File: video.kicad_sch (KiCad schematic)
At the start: 8 parts, among them U20 THS7374

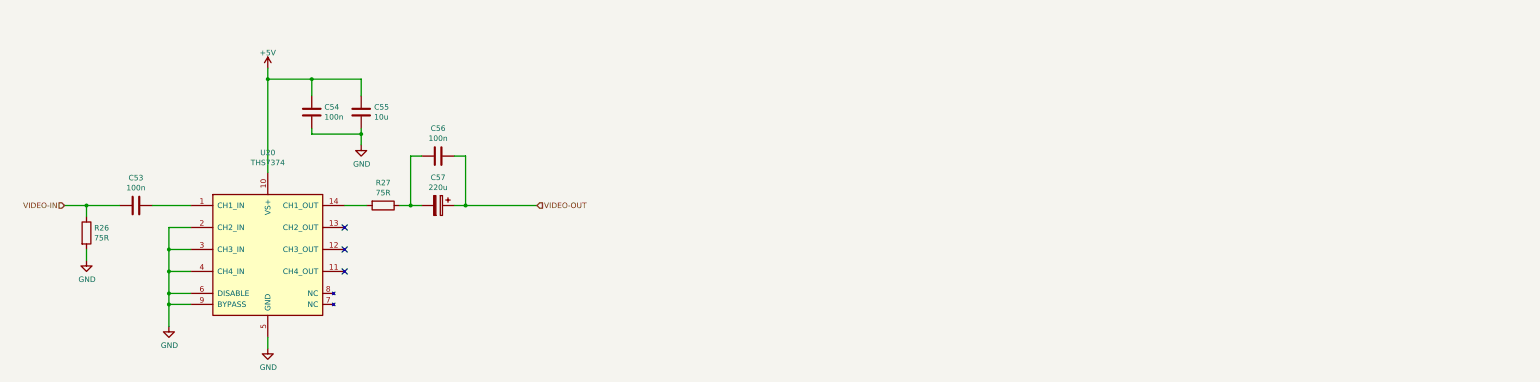
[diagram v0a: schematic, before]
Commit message: rev2 sent to fab
Added CHR RAM.
Changed board to 4 layers (was 2 layers).
Changed passives to 0603 (was 0402)
Fixed CIRAM-A10 not being hooked up
Fixed PPU-A10..A12 being hooked to VRAM but should have been.
Added more silkscreen for easier debugging.
Added filter inductor to 5V from USB-C.
Changed video out to stock (was THS7374)
Changed audio circuit to stock (was headphone amp IC)
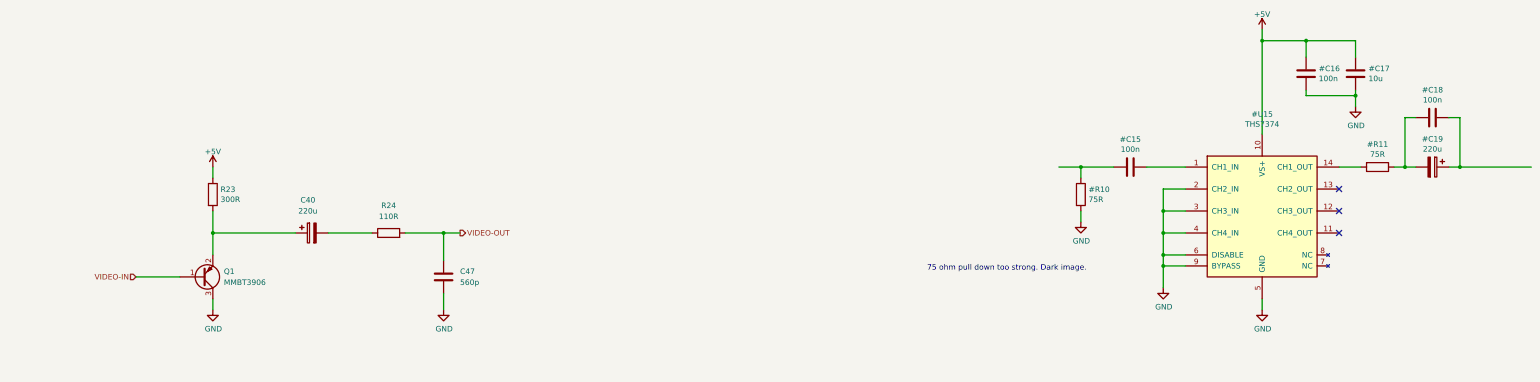
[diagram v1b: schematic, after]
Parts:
- added C40: 220u, Capacitor_Tantalum_SMD:CP_EIA-7343-15_Kemet-W, symbol Device:C_Polarized
- added C47: 560p, Capacitor_SMD:C_0603_1608Metric_Pad1.08x0.95mm_HandSolder, symbol Device:C
- added Q1: MMBT3906, Package_TO_SOT_SMD:SOT-23, symbol Transistor_BJT:MMBT3906
- added R23: 300R, Resistor_SMD:R_0603_1608Metric_Pad0.98x0.95mm_HandSolder, symbol Device:R
- added R24: 110R, Resistor_SMD:R_0603_1608Metric_Pad0.98x0.95mm_HandSolder, symbol Device:R
- #C15: renamed from C53; footprint Capacitor_SMD:C_0402_1005Metric -> Capacitor_SMD:C_0603_1608Metric_Pad1.08x0.95mm_HandSolder; Digikey 1276-1509-2-ND -> (none); MPN CL05B104KO5NNWC -> (none)
- #C16: renamed from C54; footprint Capacitor_SMD:C_0402_1005Metric -> Capacitor_SMD:C_0603_1608Metric_Pad1.08x0.95mm_HandSolder; Digikey 1276-1509-2-ND -> (none); MPN CL05B104KO5NNWC -> (none)
- #C17: renamed from C55; footprint Capacitor_SMD:C_0805_2012Metric -> Capacitor_SMD:C_0805_2012Metric_Pad1.18x1.45mm_HandSolder
- #C18: renamed from C56; footprint Capacitor_SMD:C_0402_1005Metric -> Capacitor_SMD:C_0603_1608Metric_Pad1.08x0.95mm_HandSolder; Digikey 1276-1509-2-ND -> (none); MPN CL05B104KO5NNWC -> (none)
- #R10: renamed from R26; footprint Resistor_SMD:R_0402_1005Metric -> Resistor_SMD:R_0603_1608Metric_Pad0.98x0.95mm_HandSolder; Digikey P75.0LCT-ND -> (none); MPN ERJ-2RKF75R0X -> (none)
- #R11: renamed from R27; footprint Resistor_SMD:R_0402_1005Metric -> Resistor_SMD:R_0603_1608Metric_Pad0.98x0.95mm_HandSolder; Digikey P75.0LCT-ND -> (none); MPN ERJ-2RKF75R0X -> (none)
- renumbered C57 to #C19, U20 to #U15
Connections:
- net +5V: now also R23.1
- net GND: now also C47.2, Q1.3 (C)
- net VIDEO-IN: now also Q1.1 (B); no longer #C15.2, #R10.1
- net VIDEO-OUT: now also C47.1, R24.2; no longer #C18.1, #C19.1
- new net: #C18.1, #C19.1
- new net: #C15.2, #R10.1
- new net: C40.1, Q1.2 (E), R23.2
- new net: C40.2, R24.1
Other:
- note added: "75 ohm pull down too strong. Dark image."

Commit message: filled out BOM
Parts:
- C40: Digikey (none) -> 478-11218-1-ND; MPN (none) -> TAJD227K010TNJV
- C47: Digikey (none) -> 399-C0603C561J5GAC7867CT-ND; MPN (none) -> C0603C561J5GAC7867
- Q1: Digikey (none) -> BC857CLT1GOSCT-ND; MPN MMBT3906 -> BC857CLT1G
- R23: Digikey (none) -> RMCF0603FT300RCT-ND; MPN (none) -> RMCF0603FT300R
- R24: Digikey (none) -> RMCF0603FT110RCT-ND; MPN (none) -> RMCF0603FT110R
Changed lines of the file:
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@@
   (title_block
     (title "InGame-NES MMC3")
-    (date "2022-06-03")
-    (rev "1")
+    (date "2022-08-02")
+    (rev "2")
     (company "Late to the Game")
   )
@@
       (effects (font (size 1.27 1.27)) hide)
     )
-    (property "Description" "" (id 4) (at 129.54 82.55 0)
-      (effects (font (size 1.27 1.27)) hide)
-    )
-    (property "Digikey" "" (id 5) (at 129.54 82.55 0)
-      (effects (font (size 1.27 1.27)) hide)
-    )
-    (property "MPN" "" (id 6) (at 129.54 82.55 0)
+    (property "Description" "RES SMD 300 OHM 1% 1/10W 0603" (id 4) (at 129.54 82.55 0)
+      (effects (font (size 1.27 1.27)) hide)
+    )
+    (property "Digikey" "RMCF0603FT300RCT-ND" (id 5) (at 129.54 82.55 0)
+      (effects (font (size 1.27 1.27)) hide)
+    )
+    (property "MPN" "RMCF0603FT300R" (id 6) (at 129.54 82.55 0)
       (effects (font (size 1.27 1.27)) hide)
     )
@@
       (effects (font (size 1.27 1.27)) hide)
     )
-    (property "Digikey" "" (id 5) (at 152.4 91.44 0)
-      (effects (font (size 1.27 1.27)) hide)
-    )
-    (property "MPN" "" (id 6) (at 152.4 91.44 0)
+    (property "Digikey" "478-11218-1-ND" (id 5) (at 152.4 91.44 0)
+      (effects (font (size 1.27 1.27)) hide)
+    )
+    (property "MPN" "TAJD227K010TNJV" (id 6) (at 152.4 91.44 0)
       (effects (font (size 1.27 1.27)) hide)
     )
@@
       (effects (font (size 1.27 1.27)) hide)
     )
-    (property "Description" "CAP CER 0.1UF 16V X7R 0603" (id 4) (at 182.88 101.6 0)
+    (property "Description" "CAP CER 560PF 50V C0G/NP0 0603" (id 4) (at 182.88 101.6 0)
       (effects (font (size 1.27 1.27)) hide)
     )
@@
       (effects (font (size 1.27 1.27)) hide)
     )
-    (property "Digikey" "" (id 6) (at 182.88 101.6 0)
-      (effects (font (size 1.27 1.27)) hide)
-    )
-    (property "MPN" "" (id 7) (at 182.88 101.6 0)
+    (property "Digikey" "399-C0603C561J5GAC7867CT-ND" (id 6) (at 182.88 101.6 0)
+      (effects (font (size 1.27 1.27)) hide)
+    )
+    (property "MPN" "C0603C561J5GAC7867" (id 7) (at 182.88 101.6 0)
       (effects (font (size 1.27 1.27)) hide)
     )
@@
       (effects (font (size 1.27 1.27)) hide)
     )
-    (property "MPN" "MMBT3906" (id 5) (at 127 101.6 0)
+    (property "MPN" "BC857CLT1G" (id 5) (at 127 101.6 0)
+      (effects (font (size 1.27 1.27)) hide)
+    )
+    (property "Digikey" "BC857CLT1GOSCT-ND" (id 6) (at 127 101.6 0)
       (effects (font (size 1.27 1.27)) hide)
     )
@@
       (effects (font (size 1.27 1.27)) hide)
     )
-    (property "Description" "" (id 4) (at 170.18 91.44 0)
-      (effects (font (size 1.27 1.27)) hide)
-    )
-    (property "Digikey" "" (id 5) (at 170.18 91.44 0)
-      (effects (font (size 1.27 1.27)) hide)
-    )
-    (property "MPN" "" (id 6) (at 170.18 91.44 0)
-      (effects (font (size 1.27 1.27)) hide)
-    )
+    (property "Description" "RES SMD 110 OHM 1% 1/10W 0603" (id 4) (at 170.18 91.44 0)
+      (effects (font (size 1.27 1.27)) hide)
+    )
+    (property "Digikey" "RMCF0603FT110RCT-ND" (id 5) (at 170.18 91.44 0)
+      (effects (font (size 1.27 1.27)) hide)
+    )
+    (property "MPN" "RMCF0603FT110R" (id 6) (at 170.18 91.44 0)
+      (effects (font (size 1.27 1.27)) hide)
+    )
